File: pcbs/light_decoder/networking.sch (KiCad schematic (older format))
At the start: 10 parts, among them J4 RJ45_LED_Shielded, J5 RJ45_LED_Shielded, Q13 2N7002, U4 MAX481E

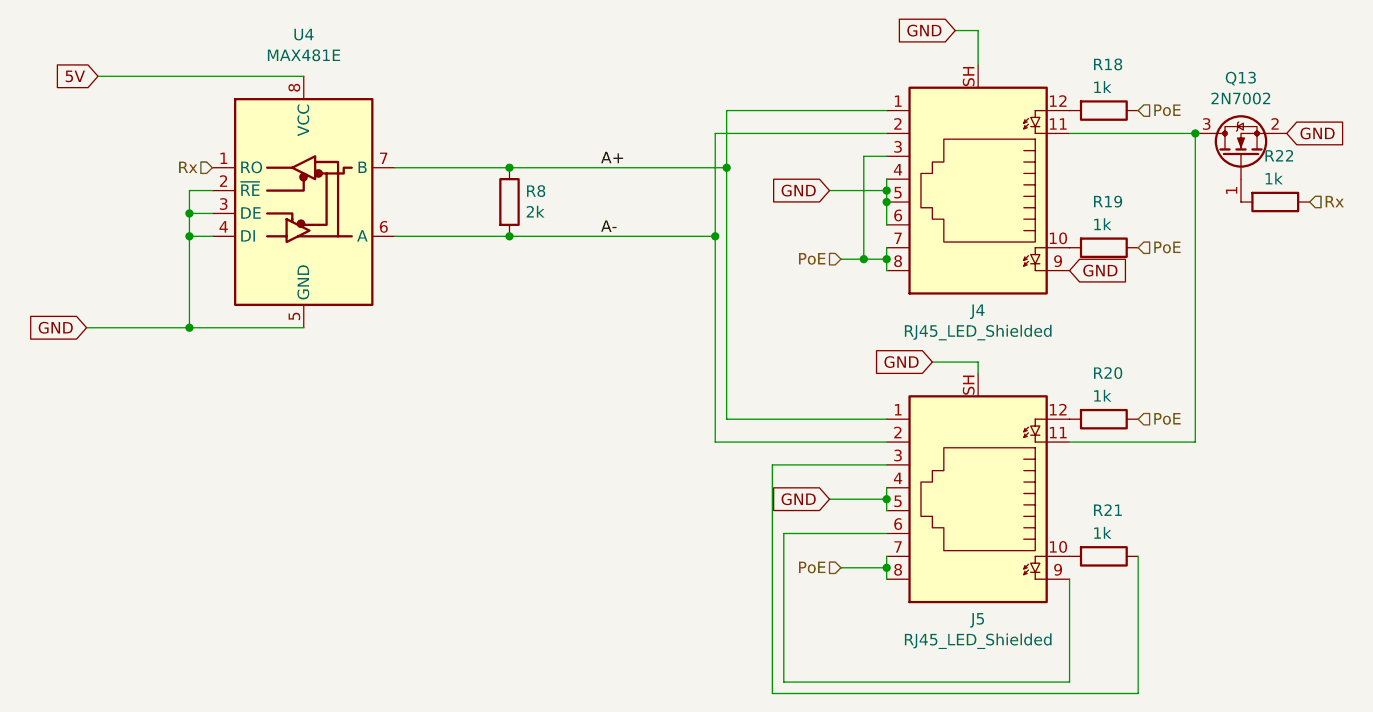
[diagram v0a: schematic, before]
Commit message: produced PCBs, dropped baudrate, removed on-board dynamic address selection - decoder must now be configured via programmer!
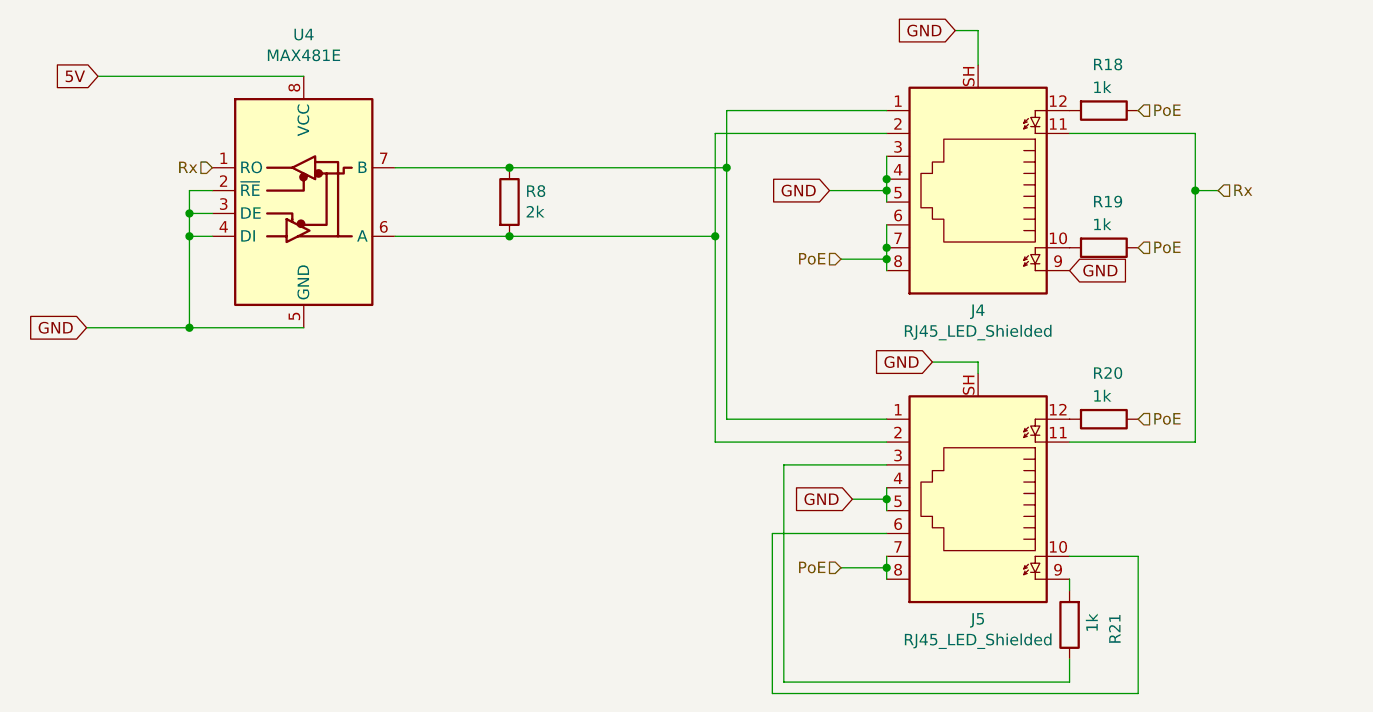
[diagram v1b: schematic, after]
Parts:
- removed Q13: 2N7002, Package_TO_SOT_SMD:SOT-23, symbol Transistor_FET:2N7002
- removed R22: 1k, Resistor_SMD:R_0603_1608Metric, symbol Device:R
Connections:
- net GND: now also J4.3; no longer J4.6
- net PoE: now also J4.6; no longer J4.3
- net Rx: now also J4.11, J5.11
- net at J5.10: now also J5.6; no longer R21.2
- net at J5.9: now also R21.2; no longer J5.6
- net A+: no longer names the net of J4.1, J5.1, R8.1, U4.7 (B)
- net A-: no longer names the net of J4.2, J5.2, R8.2, U4.6 (A)
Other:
- moved on the sheet: R21
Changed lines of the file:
@@
 	5300 3850 5300 2750
 Connection ~ 5300 2750
-Text Label 4750 2750 0    50   ~ 0
-A+
-Text Label 4750 3050 0    50   ~ 0
-A-
 Wire Wire Line
 	5300 2500 6000 2500
@@
 	6000 4550 6000 4500
 Wire Wire Line
-	6000 4200 5750 4200
+	6000 4200 5850 4200
 Connection ~ 6000 4200
-Text GLabel 5750 4200 0    50   Input ~ 0
+Text GLabel 5850 4200 0    50   Input ~ 0
 GND
 Text GLabel 5750 2850 0    50   Input ~ 0
@@
 Wire Wire Line
 	6000 3100 6000 3150
-Wire Wire Line
-	5800 3150 5900 3150
 Connection ~ 6000 3150
 Wire Wire Line
@@
 Wire Wire Line
 	2500 3450 2950 3450
-$Comp
-L Connector:RJ45_LED_Shielded J4
-U 1 1 60AE9919
-P 6400 2800
-F 0 "J4" H 6400 3375 50  0000 C CNN
-F 1 "RJ45_LED_Shielded" H 6400 3466 50  0000 C CNN
-F 2 "customs:RND_RJ45_LED" V 6400 2825 50  0001 C CNN
-F 3 "~" V 6400 2825 50  0001 C CNN
-	1    6400 2800
-	-1   0    0    1
-$EndComp
 $Comp
 L Connector:RJ45_LED_Shielded J5
@@
 Text GLabel 6800 3200 2    50   Input ~ 0
 GND
-Text GLabel 7750 2600 2    50   Input ~ 0
-GND
 $Comp
 L Device:R R18
@@
 Text HLabel 7100 2500 2    50   Input ~ 0
 PoE
-$Comp
-L Transistor_FET:2N7002 Q13
-U 1 1 60AFE446
-P 7550 2700
-F 0 "Q13" V 7892 2700 50  0000 C CNN
-F 1 "2N7002" V 7801 2700 50  0000 C CNN
-F 2 "Package_TO_SOT_SMD:SOT-23" H 7750 2625 50  0001 L CIN
-F 3 "https://www.onsemi.com/pub/Collateral/NDS7002A-D.PDF" H 7550 2700 50  0001 L CNN
-	1    7550 2700
-	0    -1   -1   0
-$EndComp
-$Comp
-L Device:R R22
-U 1 1 60B04F46
-P 7700 2900
-F 0 "R22" V 7500 2850 50  0000 L CNN
-F 1 "1k" V 7600 2850 50  0000 L CNN
-F 2 "Resistor_SMD:R_0603_1608Metric" V 7630 2900 50  0001 C CNN
-F 3 "~" H 7700 2900 50  0001 C CNN
-	1    7700 2900
-	0    1    1    0
-$EndComp
 Wire Wire Line
 	7350 2600 6800 2600
-Text HLabel 7850 2900 2    50   Input ~ 0
+Text HLabel 7450 2850 2    50   Input ~ 0
 Rx
-Wire Wire Line
-	6000 2700 5900 2700
-Wire Wire Line
-	5900 2700 5900 3150
-Connection ~ 5900 3150
-Wire Wire Line
-	5900 3150 6000 3150
-Wire Wire Line
-	6000 3000 6000 2900
-Connection ~ 6000 2900
 $Comp
 L Device:R R21
 U 1 1 60B07AA6
-P 6950 4450
-F 0 "R21" V 6750 4400 50  0000 L CNN
-F 1 "1k" V 6850 4400 50  0000 L CNN
-F 2 "Resistor_SMD:R_0603_1608Metric" V 6880 4450 50  0001 C CNN
-F 3 "~" H 6950 4450 50  0001 C CNN
-	1    6950 4450
-	0    1    1    0
+P 6800 4750
+F 0 "R21" V 6600 4700 50  0000 L CNN
+F 1 "1k" V 6700 4700 50  0000 L CNN
+F 2 "Resistor_SMD:R_0603_1608Metric" V 6730 4750 50  0001 C CNN
+F 3 "~" H 6800 4750 50  0001 C CNN
+	1    6800 4750
+	-1   0    0    1
 $EndComp
-Wire Wire Line
-	6800 4550 6800 5000
 Wire Wire Line
 	6800 5000 5550 5000
 Wire Wire Line
-	5550 5000 5550 4350
-Wire Wire Line
-	5550 4350 6000 4350
-Wire Wire Line
-	6000 4050 5500 4050
-Wire Wire Line
-	5500 4050 5500 5050
-Wire Wire Line
-	5500 5050 7100 5050
+	6000 4050 5550 4050
 Wire Wire Line
 	7100 5050 7100 4450
@@
 	6800 3950 7350 3950
 Wire Wire Line
-	7350 3950 7350 2600
-Connection ~ 7350 2600
+	7350 3950 7350 2850
+$Comp
+L Connector:RJ45_LED_Shielded J4
+U 1 1 60AE9919
+P 6400 2800
+F 0 "J4" H 6400 3375 50  0000 C CNN
+F 1 "RJ45_LED_Shielded" H 6400 3466 50  0000 C CNN
+F 2 "customs:RND_RJ45_LED" V 6400 2825 50  0001 C CNN
+F 3 "~" V 6400 2825 50  0001 C CNN
+	1    6400 2800
+	-1   0    0    1
+$EndComp
+Wire Wire Line
+	6000 3100 6000 3000
+Connection ~ 6000 3100
+Wire Wire Line
+	5800 3150 6000 3150
+Wire Wire Line
+	6000 2700 6000 2800
+Connection ~ 6000 2800
+Wire Wire Line
+	7450 2850 7350 2850
+Connection ~ 7350 2850
+Wire Wire Line
+	7350 2850 7350 2600
+Wire Wire Line
+	6800 4550 6800 4600
+Wire Wire Line
+	6800 4900 6800 5000
+Wire Wire Line
+	5500 5050 7100 5050
+Wire Wire Line
+	6800 4450 7100 4450
+Wire Wire Line
+	5550 4050 5550 5000
+Wire Wire Line
+	6000 4350 5500 4350
+Wire Wire Line
+	5500 4350 5500 5050
 $EndSCHEMATC
